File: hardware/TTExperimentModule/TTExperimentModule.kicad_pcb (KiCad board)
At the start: 4 copper layers, 45 x 30 mm, 92 parts, among them J1 Conn_01x03, J2 Conn_01x02, J3 5050700622, J5 Conn_01x04, J6 Conn_01x02, U1 74CBTLV3257, U2 AP2112K-1.8, U3 AP2112K-3.3, U4 Openframe_QFN_TT06_REV2, U5 RP2040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

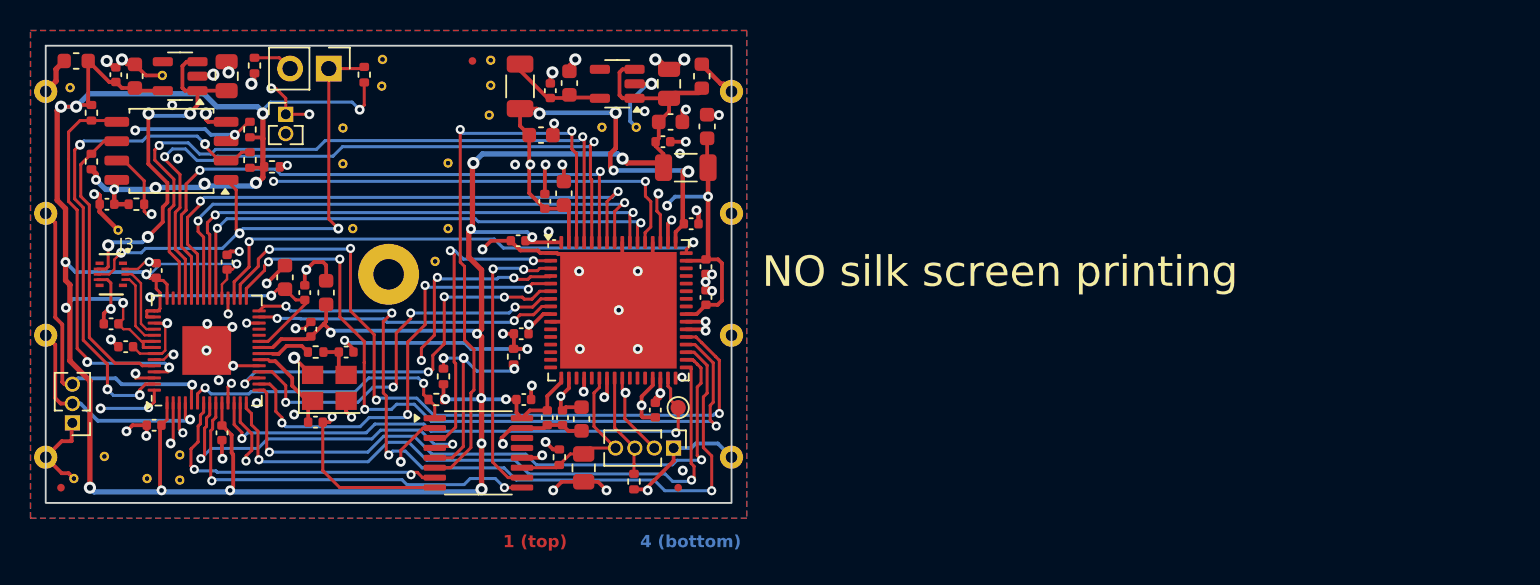
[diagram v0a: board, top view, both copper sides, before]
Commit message: reduced-height flash (dual footprint), layout rework, markings
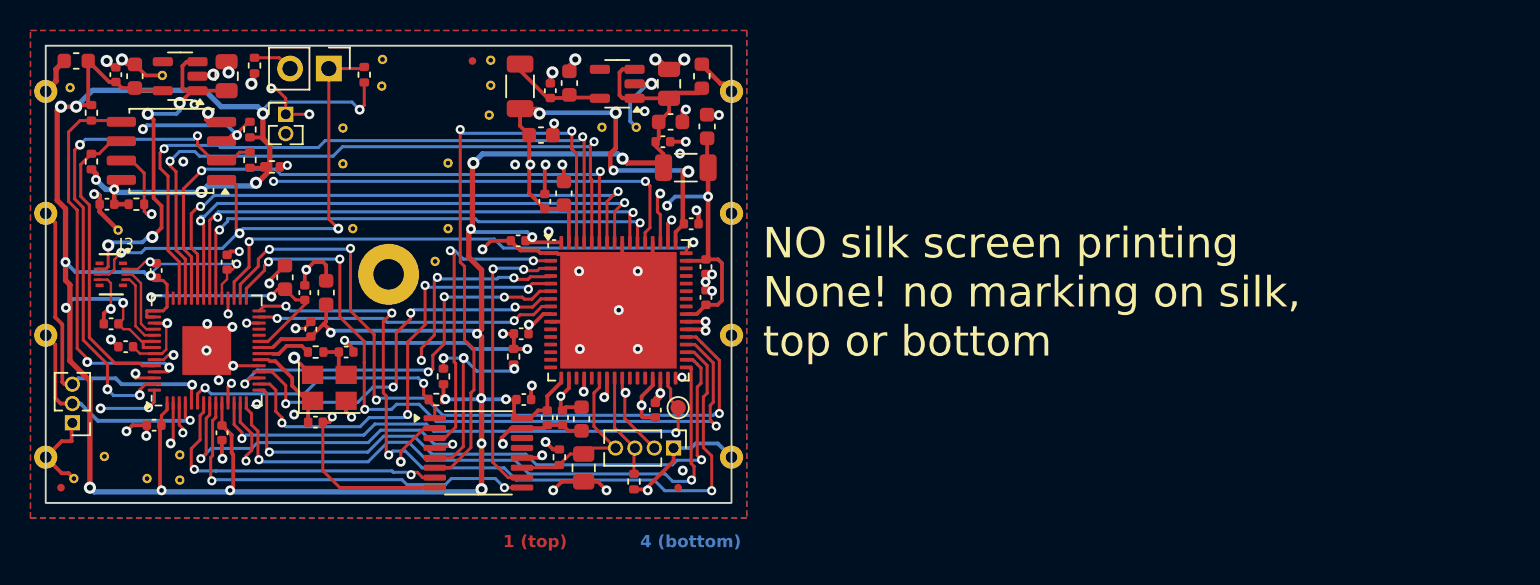
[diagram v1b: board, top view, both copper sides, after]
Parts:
- added G***: LOGO, spasic:tt_logo_mask, F.Cu at (40.9, 23.4)
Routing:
- net GND: track 178.3 -> 185.2 mm
- net /~{proj_rst}: track 65.1 -> 63.6 mm
- net /uio7: track 46.7 -> 45.3 mm
- net /uio6: track 46.0 -> 44.8 mm
- net +5V: track 24.3 -> 23.7 mm
- net /proj_clk: track 61.6 -> 61.1 mm
- net +3V3: track 241.1 -> 240.8 mm, vias 29 -> 28
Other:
- board text added: "2025 PATD"
- board text added: "4-layer stack-up, 1.0mm thickness, ENIG finish, No Markings Countour milling to create half-vias/castellated edges PCBA with 60/40 % tin-lead eutectic"
- board text added: "NO silk screen printing None! no marking on silk, top or bottom"
- board text added: "SpASIC"
- board text removed: "4-layer stack-up, 1.2mm thickness Countour milling to create half-vias/castellated edges PCBA with 60/40 % tin-lead eutectic"
- board text removed: "NO silk screen printing"
